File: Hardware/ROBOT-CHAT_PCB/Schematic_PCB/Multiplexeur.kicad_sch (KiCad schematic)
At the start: 22 parts, among them J10 Conn_01x02, J11 Conn_01x02, J12 Conn_01x02, J9 Conn_01x02, U2 TCA9546AD

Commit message: current schematic
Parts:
- J10, J11, J12, J9: footprint (none) -> Connector_JST:JST_PH_B2B-PH-K_1x02_P2.00mm_Vertical
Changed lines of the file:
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@@
 			)
 		)
-		(property "Footprint" ""
+		(property "Footprint" "Connector_JST:JST_PH_B2B-PH-K_1x02_P2.00mm_Vertical"
 			(at 116.84 132.08 0)
 			(effects
@@
 			)
 		)
-		(property "Footprint" ""
+		(property "Footprint" "Connector_JST:JST_PH_B2B-PH-K_1x02_P2.00mm_Vertical"
 			(at 193.04 132.08 0)
 			(effects
@@
 			)
 		)
-		(property "Footprint" ""
+		(property "Footprint" "Connector_JST:JST_PH_B2B-PH-K_1x02_P2.00mm_Vertical"
 			(at 231.14 132.08 0)
 			(effects
@@
 			)
 		)
-		(property "Footprint" ""
+		(property "Footprint" "Connector_JST:JST_PH_B2B-PH-K_1x02_P2.00mm_Vertical"
 			(at 154.94 132.08 0)
 			(effects

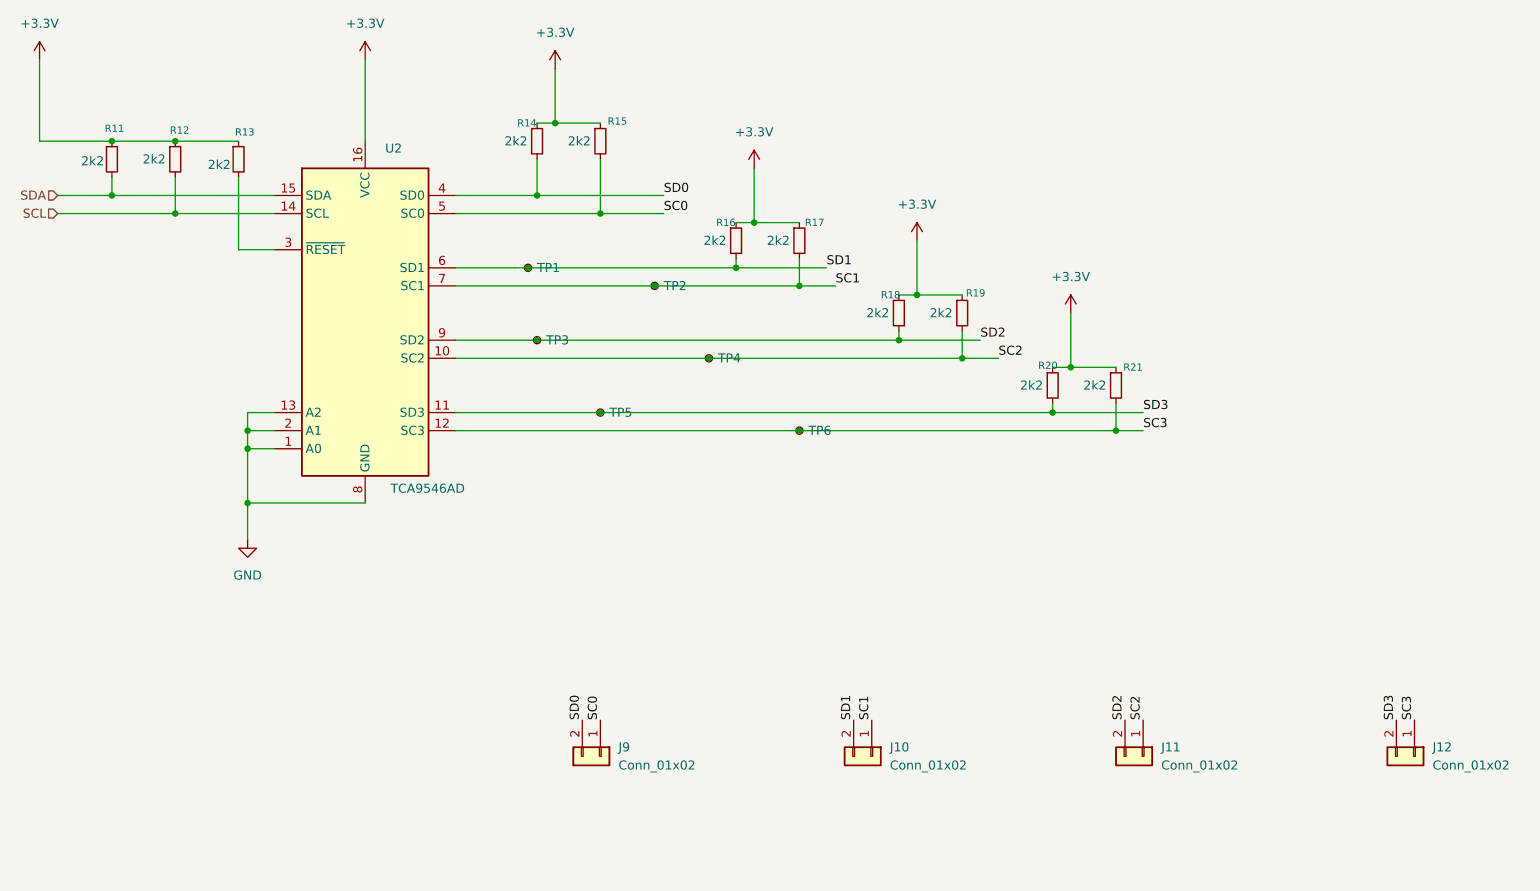
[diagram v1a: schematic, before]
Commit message: Rerouting avec Mr Fiack
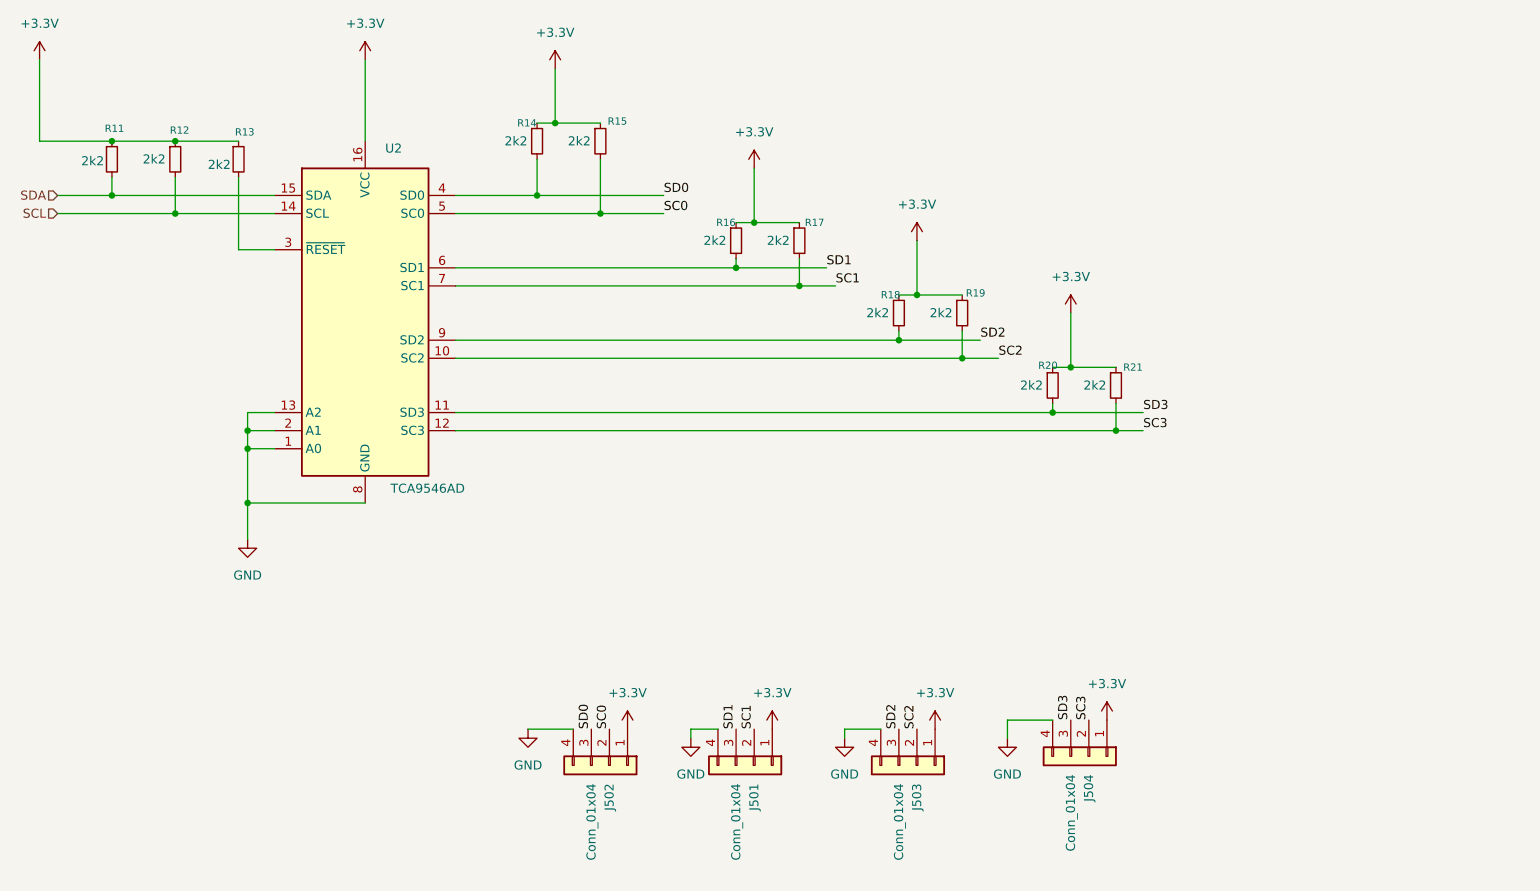
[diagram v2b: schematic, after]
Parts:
- removed J10, J11, J12, J9: Conn_01x02, Connector_JST:JST_PH_B2B-PH-K_1x02_P2.00mm_Vertical, symbol Connector_Generic:Conn_01x02
- removed TP1, TP2, TP3, TP4, TP5, TP6: TestPoint_Small, TestPoint:TestPoint_Pad_D1.5mm, symbol Connector:TestPoint_Small
- added J501, J502, J503, J504: Conn_01x04, Connector_JST:JST_PH_B4B-PH-K_1x04_P2.00mm_Vertical, symbol Connector_Generic:Conn_01x04
- R11, R12, R13, R14, R15, R16, R17, R18, R19, R20, R21: footprint Resistor_SMD:R_0603_1608Metric -> Resistor_SMD:R_0402_1005Metric
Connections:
- net +3.3V: now also J501.1 (Pin_1), J502.1 (Pin_1), J503.1 (Pin_1), J504.1 (Pin_1)
- net GND: now also J501.4 (Pin_4), J502.4 (Pin_4), J503.4 (Pin_4), J504.4 (Pin_4)
- net SC0: now also J502.2 (Pin_2)
- net SC1: now also J501.2 (Pin_2)
- net SC2: now also J503.2 (Pin_2)
- net SC3: now also J504.2 (Pin_2)
- net SD0: now also J502.3 (Pin_3)
- net SD1: now also J501.3 (Pin_3)
- net SD2: now also J503.3 (Pin_3)
- net SD3: now also J504.3 (Pin_3)
